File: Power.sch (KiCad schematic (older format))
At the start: 3 parts, among them U101 LD1117S50TR_SOT223

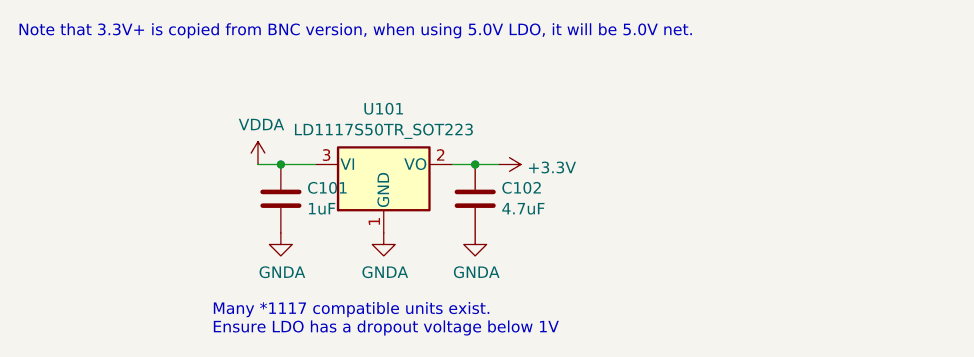
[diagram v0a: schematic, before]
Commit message: Fixed 1117 PN to LDL1117S50R
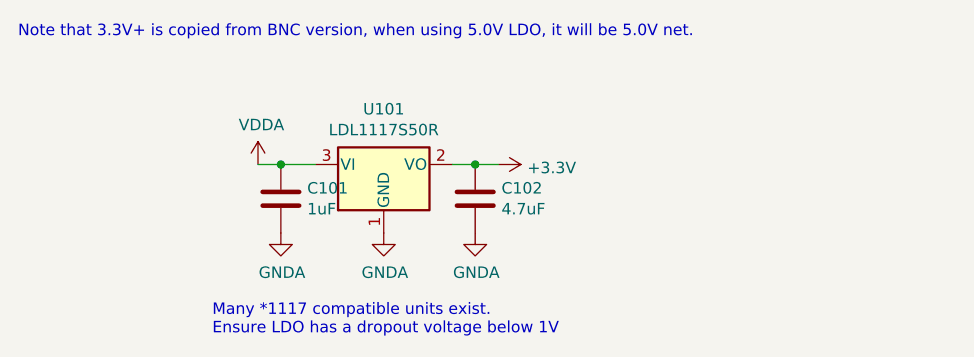
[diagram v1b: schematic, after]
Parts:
- U101: value LD1117S50TR_SOT223 -> LDL1117S50R
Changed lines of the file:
@@
 P 2400 1300
 F 0 "U101" H 2400 1542 50  0000 C CNN
-F 1 "LD1117S50TR_SOT223" H 2400 1451 50  0000 C CNN
+F 1 "LDL1117S50R" H 2400 1451 50  0000 C CNN
 F 2 "Package_TO_SOT_SMD:SOT-223-3_TabPin2" H 2400 1500 50  0001 C CNN
 F 3 "http://www.st.com/st-web-ui/static/active/en/resource/technical/document/datasheet/CD00000544.pdf" H 2500 1050 50  0001 C CNN
